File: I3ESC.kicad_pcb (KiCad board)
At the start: 4 copper layers, 74 x 54 mm, 187 parts, among them J1 JST SR/SZ, J10 VIN_BARREL, J11 Barrel_Jack, J12 JST SR/SZ, J13 Conn_01x04, J2 Screw_Terminal_01x02, J3 Screw_Terminal_01x02, J4 Screw_Terminal_01x02, J5 Conn_01x06, J6 Wireless Coil, J7 VIN_TERMINAL, J8 Conn_01x06, J9 JST SR/SZ, SW2 boot-red, SW3 user1-white, U1 SY8113BADC, U10 USBLC6-2P6, U11 IP6826, U12 FD8288T (DRV8300), U2 FD8288T (DRV8300), U3 SPX3819M5-L-3-3, U4 STM32G474RETx, U5 Qwiic1, U6 USB_C_Receptacle, U8 ABM3B-8.000MHZ, U9 USB_C_Receptacle

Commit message: push before schematic cleanup
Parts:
- removed TP5: TP_CC2, AlfredoFootprints:GE_TestPoint_Loop
- removed TP6: TP_CC1, AlfredoFootprints:GE_TestPoint_Loop
- C27, C28, C30, C31, C32: footprint Capacitor_SMD:C_0402_1005Metric -> Capacitor_SMD:C_0603_1608Metric
- D7: value LED_RED -> LED_YELLOW
- D9: value LED_Red -> LED_YELLOW
- R20, R26, R27, R28, R29, R34, R35, R9: footprint Resistor_SMD:R_0402_1005Metric -> Resistor_SMD:R_0603_1608Metric
- moved TP3 75.5 mm to (-21.4, -13.4)
- moved C11 54.7 mm to (9.30, -14.8)
- moved C13 54.7 mm to (9.30, -12.9)
- moved U3 54.7 mm to (12.2, -13.9)
- moved D10 42.9 mm to (33.7, 6.70), turned to 90 degrees
- moved D9 42.9 mm to (35.5, 6.70), turned to 90 degrees
- moved R28 40.3 mm to (35.4, 3.20), turned to 90 degrees
- moved R29 40.0 mm to (33.8, 3.10), turned to 90 degrees
- moved TP2 30.7 mm to (48.5, 0.20)
- moved TP1 30.7 mm to (48.5, 2.60)
- moved C27 28.1 mm to (38.0, 2.50), turned to 0 degrees
- moved C28 28.1 mm to (40.9, 2.50), turned to 180 degrees
- moved U11 28.0 mm to (38.9, -2.42)
- moved C36 27.7 mm to (44.3, -6.10), turned to -90 degrees
- moved R27 27.6 mm to (33.6, -8.90), turned to 90 degrees
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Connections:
- J11 pad 1: /IE-FETS-2B/SHx -> /IE-FETS-2C/SHx
- J11 pad 2: /IE-FETS-2C/SHx -> /IE-FETS-2B/SHx
- J8 pad 2: TEMP_2 -> OPAMP5_VOUT
- U11 pad 8: Net-(U11-CC1) -> Qi_CC1
- U11 pad 9: Net-(U11-CC2) -> Qi_CC2
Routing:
- net +5V: track 8.30 -> 173.2 mm, vias 0 -> 2
- net ENC_2A: track 0.00 -> 93.3 mm, vias 0 -> 1
- net ENC_2B: track 0.00 -> 90.6 mm, vias 0 -> 1
- net ENC_2C: track 0.00 -> 82.2 mm, vias 0 -> 1
- net OPAMP5_VOUT: track 0.00 -> 66.0 mm, vias 0 -> 1
- net +3V3: track 110.1 -> 163.5 mm, vias 13 -> 21
- net GND: track 50.7 -> 99.5 mm, vias 99 -> 160
- net VCC: track 30.3 -> 68.7 mm
- net /IE-FETS-2B/SHx: track 48.5 -> 72.2 mm
- net V_DETECT: track 0.00 -> 23.7 mm, vias 0 -> 2
- net Net-(J6-Pin_1): track 0.00 -> 23.1 mm
- net /V_USB: track 0.00 -> 21.7 mm, vias 0 -> 8
- net /IE-FETS-2A/GLx: track 0.00 -> 17.4 mm, vias 0 -> 2
- net /IE-FETS-2A/GHx: track 0.00 -> 17.3 mm, vias 0 -> 2
- net Net-(JP1-B): track 0.00 -> 17.2 mm
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- added copper zone on B.Cu, net /PGND
- added copper zone on F.Cu, net /PGND
- added copper zone on F.Cu, net /V_QI_USB
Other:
- board size 74 x 54 mm -> 82 x 54 mm
- board text added: "3V3"
- board text added: "SCL"
- board text added: "SDA"

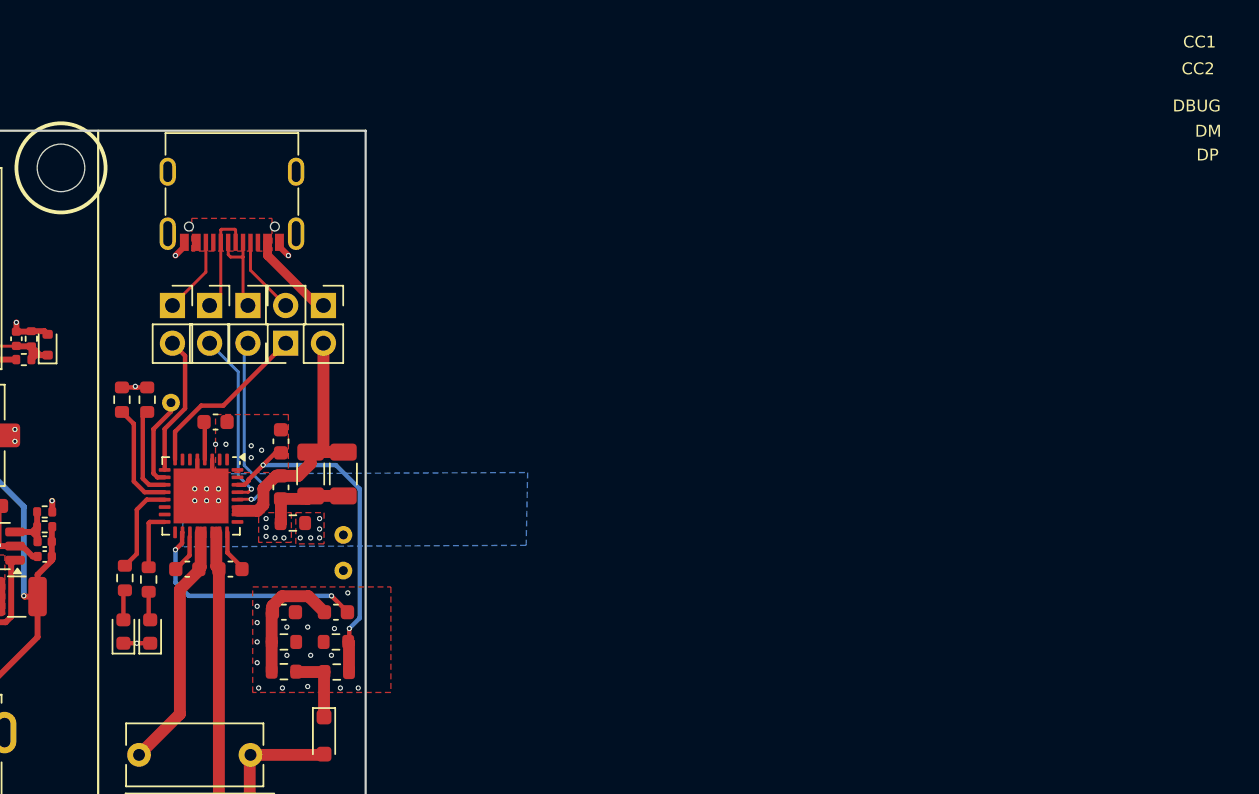
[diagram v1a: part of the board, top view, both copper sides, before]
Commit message: schematic fix before re-org
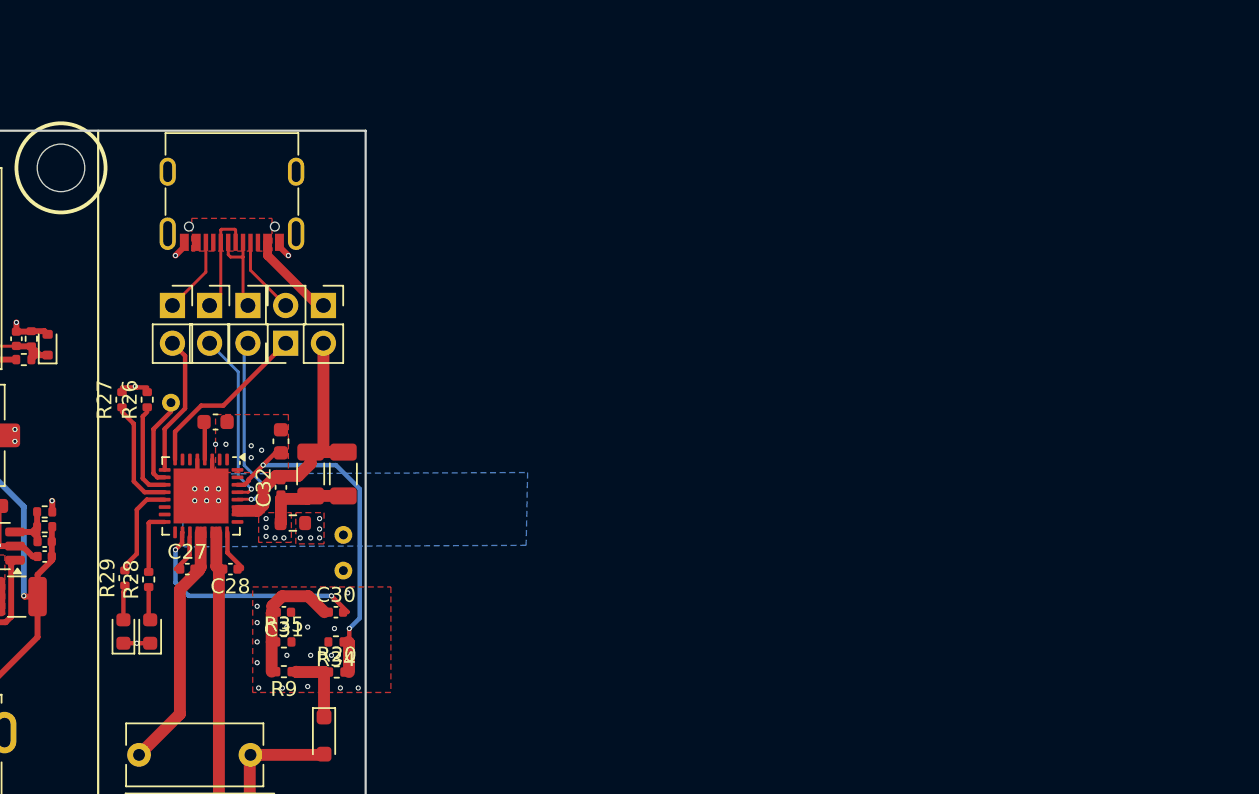
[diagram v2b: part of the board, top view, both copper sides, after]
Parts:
- C27, C28, C30, C31, C32: footprint Capacitor_SMD:C_0603_1608Metric -> Capacitor_SMD:C_0402_1005Metric
- D7: value LED_YELLOW -> LED_RED
- D9: value LED_YELLOW -> LED_Red
- R20, R26, R27, R28, R29, R34, R35, R9: footprint Resistor_SMD:R_0603_1608Metric -> Resistor_SMD:R_0402_1005Metric
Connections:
- J8 pad 2: OPAMP5_VOUT -> TEMP_2
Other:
- board text removed: "CC1"
- board text removed: "CC2"
- board text removed: "DBUG"
- board text removed: "DM"
- board text removed: "DP"

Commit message: cleaned up all files, created schematic PDF
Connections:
- net /PGND renamed /IE-QI-WIRELESS/PGND
- net /V_QI_USB renamed /IE-QI-WIRELESS/V_QI_USB

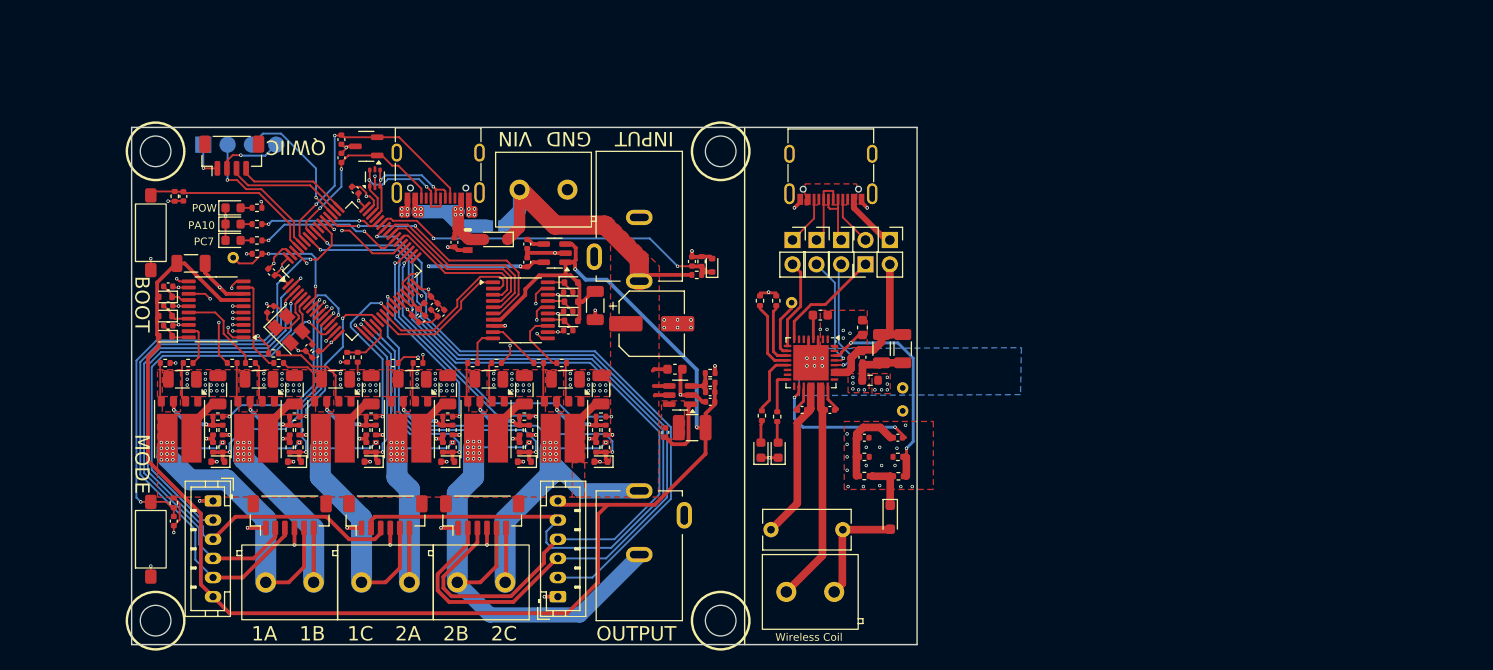
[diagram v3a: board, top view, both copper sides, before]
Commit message: Refactor net naming and update component values
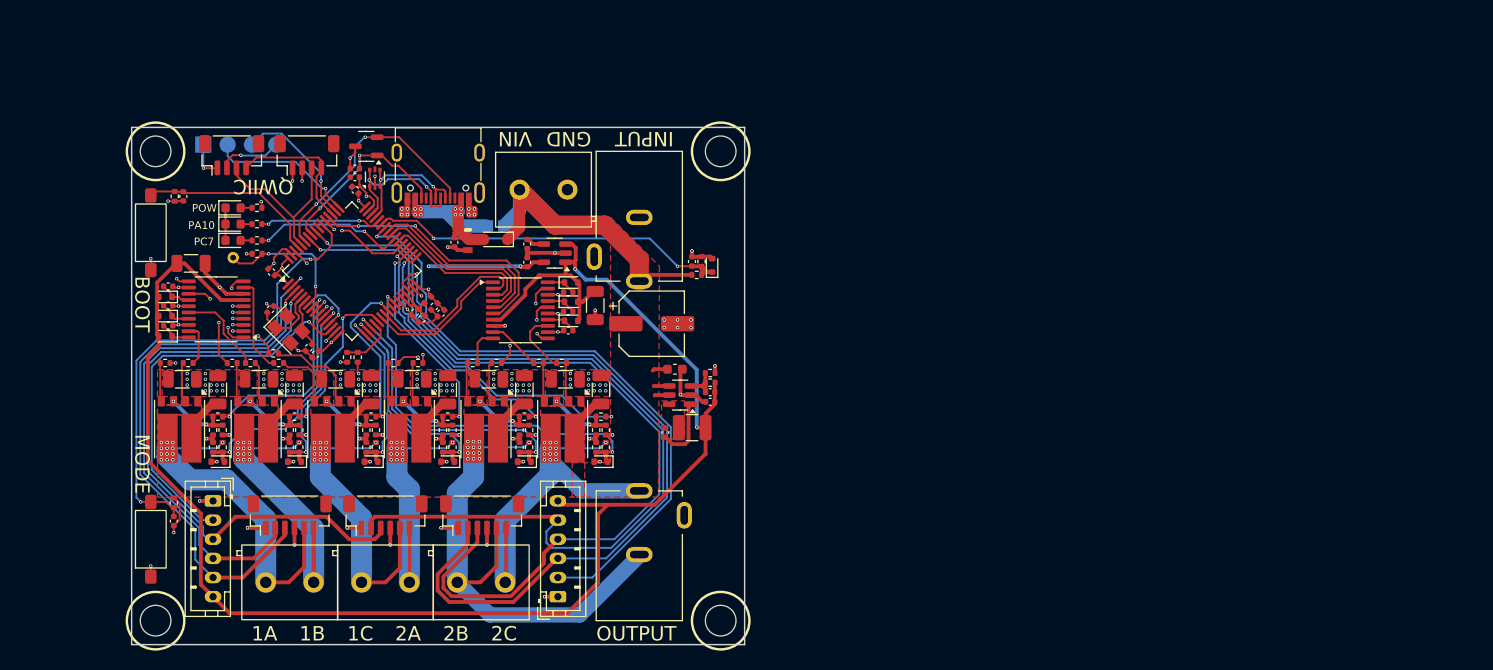
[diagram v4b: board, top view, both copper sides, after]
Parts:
- removed C27, C28, C32: 100nF, 50V, Capacitor_SMD:C_0402_1005Metric
- removed C29: 250nF, 100V, Capacitor_THT:C_Rect_L9.0mm_W4.0mm_P7.50mm_MKT
- removed C30, C31: 15nF, Capacitor_SMD:C_0402_1005Metric
- removed C33, C34: 10uF, 50V, Capacitor_SMD:C_1206_3216Metric
- removed C35, C36: 2.2uF, 50V, Capacitor_SMD:C_0603_1608Metric
- removed D10: LED_Green, LED_SMD:LED_0603_1608Metric
- removed D14: 1N5819, AlfredoFootprints:D_SOD-323
- removed D9: LED_Red, LED_SMD:LED_0603_1608Metric
- removed J6: Wireless Coil, AlfredoFootprints:TerminalBlock_Ningbo_2P_5mm
- removed JP1: Qi_Enable, Connector_PinSocket_2.54mm:PinSocket_1x02_P2.54mm_Vertical
- removed JP4: Qi_D-, Connector_PinSocket_2.54mm:PinSocket_1x02_P2.54mm_Vertical
- removed JP5: Qi_D+, Connector_PinSocket_2.54mm:PinSocket_1x02_P2.54mm_Vertical
- removed JP6: Qi_CC2, Connector_PinSocket_2.54mm:PinSocket_1x02_P2.54mm_Vertical
- removed JP7: Qi_CC1, Connector_PinSocket_2.54mm:PinSocket_1x02_P2.54mm_Vertical
- removed R20, R26, R27: 100K, Resistor_SMD:R_0402_1005Metric
- removed R28, R29: 1K, Resistor_SMD:R_0402_1005Metric
- removed R33: 20mR, Resistor_SMD:R_0603_1608Metric
- removed R34: 10K, Resistor_SMD:R_0402_1005Metric
- removed R35: 33K, Resistor_SMD:R_0402_1005Metric
- removed R9: 3K3, Resistor_SMD:R_0402_1005Metric
- removed TP1: GND, AlfredoFootprints:GE_TestPoint_Loop
- removed TP2: QI_PGND, AlfredoFootprints:GE_TestPoint_Loop
- removed TP4: TP_DEBUG, AlfredoFootprints:GE_TestPoint_Loop
- removed U11: IP6826, Package_DFN_QFN:QFN-32-1EP_5x5mm_P0.5mm_EP3.7x3.7mm
- removed U6: USB_C_Receptacle, AlfredoFootprints:USB_TYPE-C-31-M-12
- added U7: Qwiic2, Connector_JST:JST_SH_BM04B-SRSS-TB_1x04-1MP_P1.00mm_Vertical, F.Cu at (-13.7, -24.1)
- J13: value Conn_01x04 -> Conn_SWD
- J5: value Conn_01x06 -> Encoder1
- J8: value Conn_01x06 -> Encoder2
- R1, R10, R11, R12, R19, R21, R3, R37, R38, R4, R6, R7: value 10R -> 0R
- moved C25 4.16 mm to (-8.70, -21.8), turned to 0 degrees
- moved C24 1.79 mm to (-8.70, -22.7), turned to 180 degrees
- moved U5 0.05 mm to (-21.6, -24.1)
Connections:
- net /IE-FETS-1A/GHx renamed /IE-PHASES/IE-FETS-1A/GHx
- net /IE-FETS-1A/GLx renamed /IE-PHASES/IE-FETS-1A/GLx
- net /IE-FETS-1B/GHx renamed /IE-PHASES/IE-FETS-1B/GHx
- net /IE-FETS-1B/GLx renamed /IE-PHASES/IE-FETS-1B/GLx
- net /IE-FETS-1C/GHx renamed /IE-PHASES/IE-FETS-1C/GHx
- net /IE-FETS-1C/GLx renamed /IE-PHASES/IE-FETS-1C/GLx
- net /IE-FETS-2A/GHx renamed /IE-PHASES/IE-FETS-2A/GHx
- net /IE-FETS-2A/GLx renamed /IE-PHASES/IE-FETS-2A/GLx
- net /IE-FETS-2B/GHx renamed /IE-PHASES/IE-FETS-2B/GHx
- net /IE-FETS-2B/GLx renamed /IE-PHASES/IE-FETS-2B/GLx
- net /IE-FETS-2C/GHx renamed /IE-PHASES/IE-FETS-2C/GHx
- net /IE-FETS-2C/GLx renamed /IE-PHASES/IE-FETS-2C/GLx
- net /V_USB renamed /IE-USB/V_USB
- C38 pad 2: /IE-FETS-2A/SHx -> /IE-PHASES/IE-FETS-2A/SHx
- C39 pad 2: /IE-FETS-2B/SHx -> /IE-PHASES/IE-FETS-2B/SHx
- C4 pad 2: /IE-FETS-1A/SHx -> /IE-PHASES/IE-FETS-1A/SHx
- C40 pad 2: /IE-FETS-2C/SHx -> /IE-PHASES/IE-FETS-2C/SHx
- C5 pad 2: /IE-FETS-1B/SHx -> /IE-PHASES/IE-FETS-1B/SHx
- C6 pad 2: /IE-FETS-1C/SHx -> /IE-PHASES/IE-FETS-1C/SHx
- J1 pad 5: /IE-FETS-1C/SHx -> /IE-PHASES/IE-FETS-1C/SHx
- J1 pad 6: /IE-FETS-2A/SHx -> /IE-PHASES/IE-FETS-2A/SHx
- J11 pad 1: /IE-FETS-2C/SHx -> /IE-PHASES/IE-FETS-2C/SHx
- J11 pad 2: /IE-FETS-2B/SHx -> /IE-PHASES/IE-FETS-2B/SHx
- J12 pad 5: /IE-FETS-2B/SHx -> /IE-PHASES/IE-FETS-2B/SHx
- J12 pad 6: /IE-FETS-2C/SHx -> /IE-PHASES/IE-FETS-2C/SHx
- J13 pad 2: SDA -> SWDIO
- J13 pad 3: SCL -> SWCLK
- J2 pad 1: /IE-FETS-1B/SHx -> /IE-PHASES/IE-FETS-1B/SHx
- J2 pad 2: /IE-FETS-1A/SHx -> /IE-PHASES/IE-FETS-1A/SHx
- J3 pad 1: /IE-FETS-2A/SHx -> /IE-PHASES/IE-FETS-2A/SHx
- J3 pad 2: /IE-FETS-1C/SHx -> /IE-PHASES/IE-FETS-1C/SHx
- J4 pad 1: /IE-FETS-2C/SHx -> /IE-PHASES/IE-FETS-2C/SHx
- J4 pad 2: /IE-FETS-2B/SHx -> /IE-PHASES/IE-FETS-2B/SHx
- J8 pad 2: TEMP_2 -> OPAMP5_VOUT
- J9 pad 5: /IE-FETS-1A/SHx -> /IE-PHASES/IE-FETS-1A/SHx
- J9 pad 6: /IE-FETS-1B/SHx -> /IE-PHASES/IE-FETS-1B/SHx
- Q1 pad 1: unconnected-(Q1-S1-Pad1) -> /IE-PHASES/IE-FETS-1B/SHx
- Q1 pad 5: /IE-FETS-1B/SHx -> /IE-PHASES/IE-FETS-1B/SHx
- Q2 pad 1: unconnected-(Q2-S1-Pad1) -> /IE-PHASES/IE-FETS-1C/SHx
- Q2 pad 5: /IE-FETS-1C/SHx -> /IE-PHASES/IE-FETS-1C/SHx
- Q3 pad 1: unconnected-(Q3-S1-Pad1) -> /IE-PHASES/IE-FETS-2A/SHx
- Q3 pad 5: /IE-FETS-2A/SHx -> /IE-PHASES/IE-FETS-2A/SHx
- Q4 pad 1: unconnected-(Q4-S1-Pad1) -> /IE-PHASES/IE-FETS-1A/SHx
- Q4 pad 5: /IE-FETS-1A/SHx -> /IE-PHASES/IE-FETS-1A/SHx
- Q5 pad 1: unconnected-(Q5-S1-Pad1) -> /IE-PHASES/IE-FETS-2B/SHx
- Q5 pad 5: /IE-FETS-2B/SHx -> /IE-PHASES/IE-FETS-2B/SHx
- Q6 pad 1: unconnected-(Q6-S1-Pad1) -> /IE-PHASES/IE-FETS-2C/SHx
- Q6 pad 5: /IE-FETS-2C/SHx -> /IE-PHASES/IE-FETS-2C/SHx
- R17 pad 2: /IE-FETS-1A/SHx -> /IE-PHASES/IE-FETS-1A/SHx
- R32 pad 2: /IE-FETS-1B/SHx -> /IE-PHASES/IE-FETS-1B/SHx
- R48 pad 2: /IE-FETS-2A/SHx -> /IE-PHASES/IE-FETS-2A/SHx
- R56 pad 2: /IE-FETS-2B/SHx -> /IE-PHASES/IE-FETS-2B/SHx
- R59 pad 2: /IE-FETS-1C/SHx -> /IE-PHASES/IE-FETS-1C/SHx
- R64 pad 2: /IE-FETS-2C/SHx -> /IE-PHASES/IE-FETS-2C/SHx
- U12 pad 12: /IE-FETS-2C/SHx -> /IE-PHASES/IE-FETS-2C/SHx
- U12 pad 15: /IE-FETS-2B/SHx -> /IE-PHASES/IE-FETS-2B/SHx
- U12 pad 18: /IE-FETS-2A/SHx -> /IE-PHASES/IE-FETS-2A/SHx
- U2 pad 12: /IE-FETS-1C/SHx -> /IE-PHASES/IE-FETS-1C/SHx
- U2 pad 15: /IE-FETS-1B/SHx -> /IE-PHASES/IE-FETS-1B/SHx
- U2 pad 18: /IE-FETS-1A/SHx -> /IE-PHASES/IE-FETS-1A/SHx
- U5 pad 3: SWCLK -> SDA
- U5 pad 4: SWDIO -> SCL
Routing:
- net /IE-PHASES/IE-FETS-2B/SHx: track 0.00 -> 72.2 mm, vias 0 -> 14
- net /IE-FETS-2B/SHx: track 72.2 -> 0.00 mm, vias 14 -> 0
- net /IE-PHASES/IE-FETS-1C/SHx: track 0.00 -> 56.0 mm, vias 0 -> 14
- net /IE-FETS-1C/SHx: track 56.0 -> 0.00 mm, vias 14 -> 0
- net /IE-PHASES/IE-FETS-2A/SHx: track 0.00 -> 55.6 mm, vias 0 -> 14
- net /IE-FETS-2A/SHx: track 55.6 -> 0.00 mm, vias 14 -> 0
- net /IE-PHASES/IE-FETS-2C/SHx: track 0.00 -> 51.4 mm, vias 0 -> 14
- net /IE-FETS-2C/SHx: track 51.4 -> 0.00 mm, vias 14 -> 0
- net /IE-PHASES/IE-FETS-1A/SHx: track 0.00 -> 49.9 mm, vias 0 -> 14
- net /IE-FETS-1A/SHx: track 49.9 -> 0.00 mm, vias 14 -> 0
- net /IE-PHASES/IE-FETS-1B/SHx: track 0.00 -> 46.9 mm, vias 0 -> 14
- net /IE-FETS-1B/SHx: track 46.9 -> 0.00 mm, vias 14 -> 0
- net V_DETECT: track 23.7 -> 0.00 mm, vias 2 -> 0
- net Net-(J6-Pin_1): track 23.1 -> 0.00 mm
- net Net-(JP1-B): track 17.2 -> 0.00 mm
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- added copper zone on F.Cu, net /IE-PHASES/IE-FETS-1A/SHx
- added copper zone on F.Cu, net /IE-PHASES/IE-FETS-1B/SHx
- added copper zone on F.Cu, net /IE-PHASES/IE-FETS-1C/SHx
- added copper zone on F.Cu, net /IE-PHASES/IE-FETS-2A/SHx
- added copper zone on F.Cu, net /IE-PHASES/IE-FETS-2B/SHx
- added copper zone on F.Cu, net /IE-PHASES/IE-FETS-2C/SHx
- removed copper zone on B.Cu, net /IE-QI-WIRELESS/PGND
- removed copper zone on F.Cu, net /IE-QI-WIRELESS/PGND
- removed copper zone on F.Cu, net /IE-QI-WIRELESS/V_QI_USB
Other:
- board size 82 x 54 mm -> 64 x 54 mm
- board text removed: "Wireless Coil"
